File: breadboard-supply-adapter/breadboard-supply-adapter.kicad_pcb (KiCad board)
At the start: 2 copper layers, 8 parts, among them J1 Conn_01x02, J2 Conn_01x02, J3 EURORACK_CONN_16_GATE_CV, J4 Conn_01x04

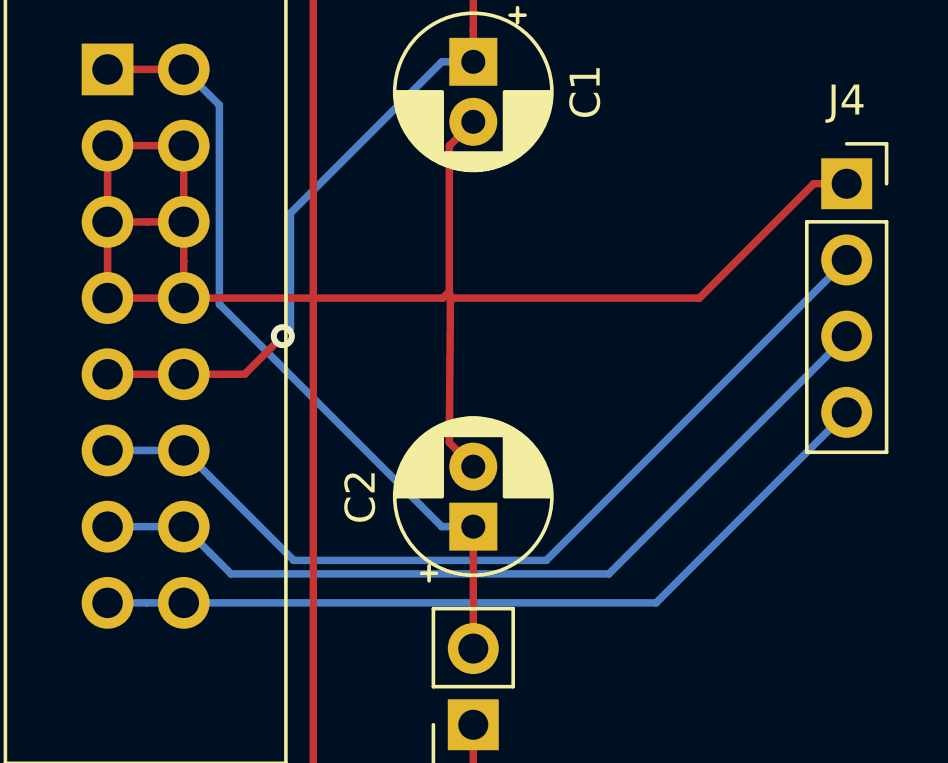
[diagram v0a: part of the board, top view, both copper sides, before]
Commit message: reversed the polarity of the neg cap (oops)
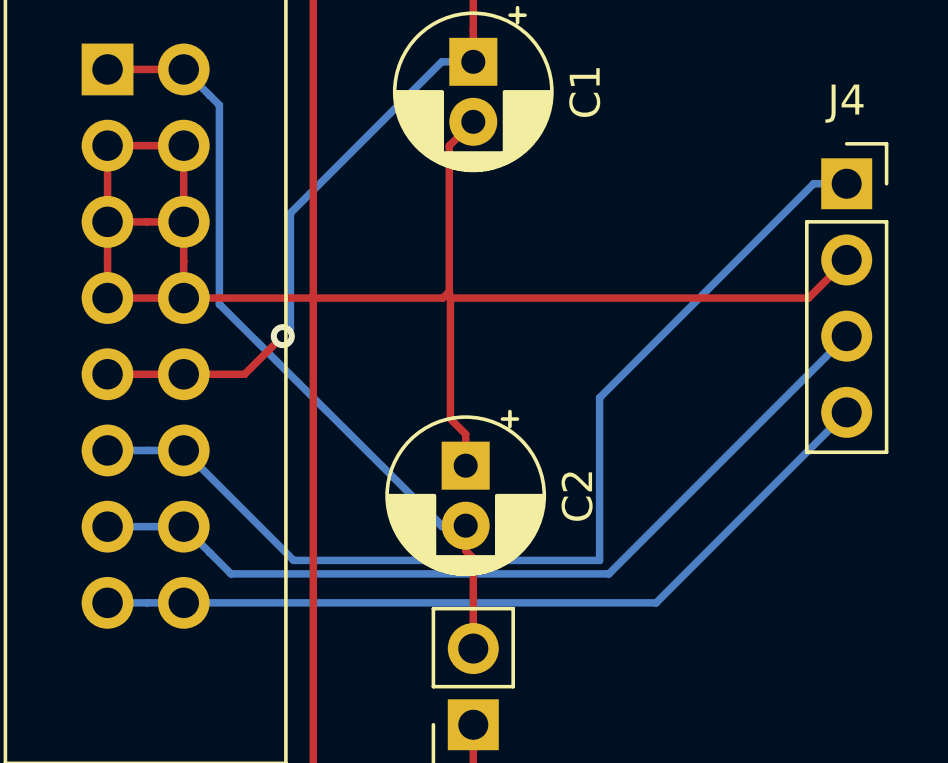
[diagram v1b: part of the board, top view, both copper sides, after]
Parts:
- moved C2 2.05 mm to (58.9, 73.2), turned to 270 degrees
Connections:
- C2 pad 1: -12V -> GND
- C2 pad 2: GND -> -12V
- J4 pad 1: GND -> Net-(J3-Pad11)
- J4 pad 2: Net-(J3-Pad11) -> GND
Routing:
- net Net-(J3-Pad11): track 30.3 -> 34.5 mm
- net GND: track 98.8 -> 97.6 mm
